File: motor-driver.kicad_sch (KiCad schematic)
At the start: 5 parts, among them J2 Conn_01x02, J3 Conn_01x02, U4 DRV8835

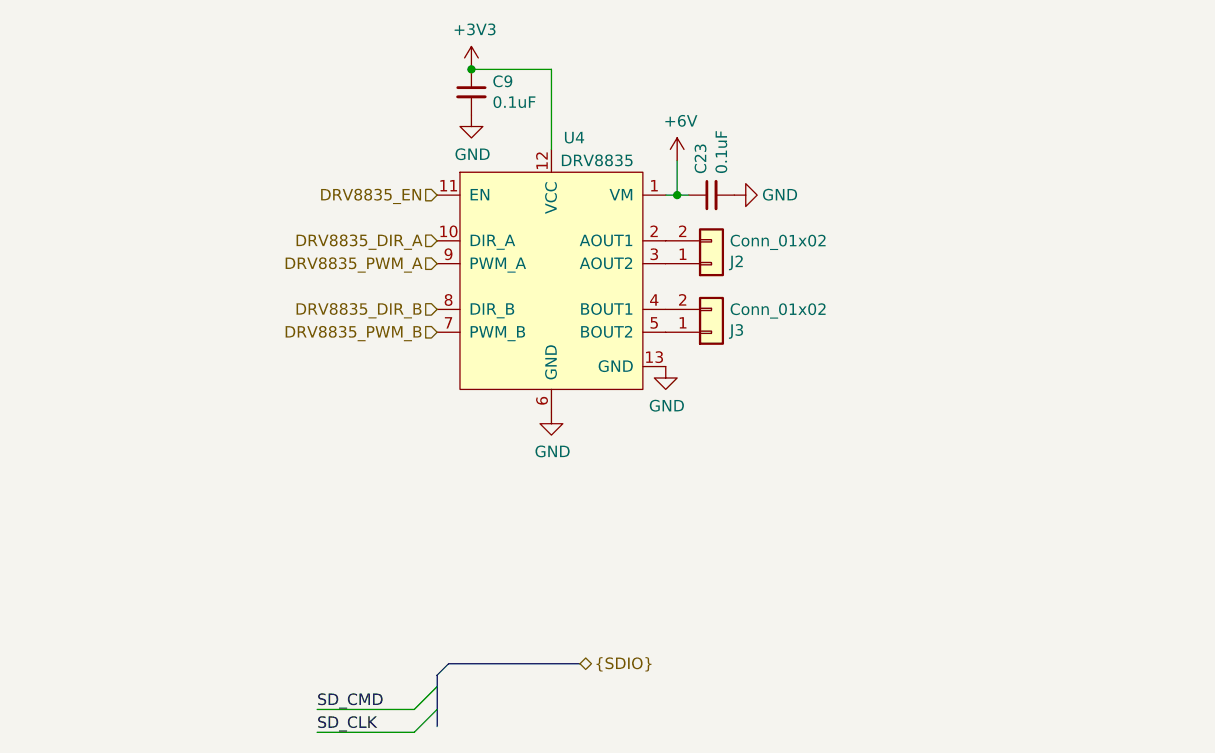
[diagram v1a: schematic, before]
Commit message: Add bus to the motor controller
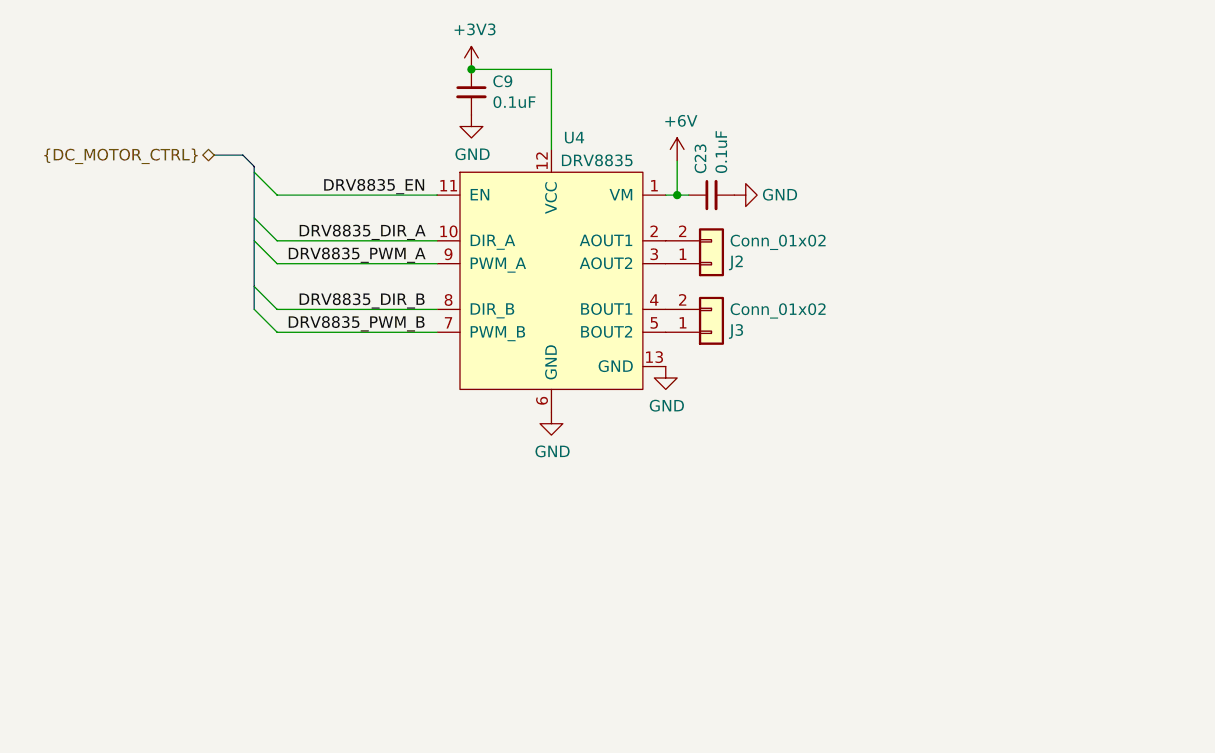
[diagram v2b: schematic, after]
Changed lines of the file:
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@@
   (junction (at 158.75 73.66) (diameter 0) (color 0 0 0 0)
   )
-  (bus_entry (at 132.08 128.27) (size -2.54 2.54)
+  (bus_entry (at 114.3 86.36) (size -2.54 -2.54)
     (stroke (width 0) (type default) (color 0 0 0 0))
   )
-  (bus_entry (at 132.08 130.81) (size -2.54 2.54)
+  (bus_entry (at 114.3 81.28) (size -2.54 -2.54)
+    (stroke (width 0) (type default) (color 0 0 0 0))
+  )
+  (bus_entry (at 114.3 78.74) (size -2.54 -2.54)
+    (stroke (width 0) (type default) (color 0 0 0 0))
+  )
+  (bus_entry (at 114.3 88.9) (size -2.54 -2.54)
+    (stroke (width 0) (type default) (color 0 0 0 0))
+  )
+  (bus_entry (at 114.3 73.66) (size -2.54 -2.54)
     (stroke (width 0) (type default) (color 0 0 0 0))
   )
@@
     (stroke (width 0) (type default) (color 0 0 0 0))
   )
-  (bus (pts (xy 132.08 130.81) (xy 132.08 132.715))
-    (stroke (width 0) (type default) (color 0 0 0 0))
-  )
   (wire (pts (xy 158.75 69.85) (xy 158.75 73.66))
     (stroke (width 0) (type default) (color 0 0 0 0))
   )
-  (bus (pts (xy 133.35 125.73) (xy 132.08 127))
+  (wire (pts (xy 132.08 81.28) (xy 114.3 81.28))
+    (stroke (width 0) (type default) (color 0 0 0 0))
+  )
+  (bus (pts (xy 111.76 70.485) (xy 111.76 71.12))
     (stroke (width 0) (type default) (color 0 0 0 0))
   )
@@
     (stroke (width 0) (type default) (color 0 0 0 0))
   )
-  (bus (pts (xy 132.08 127) (xy 132.08 128.27))
+  (bus (pts (xy 111.76 83.82) (xy 111.76 86.36))
+    (stroke (width 0) (type default) (color 0 0 0 0))
+  )
+  (bus (pts (xy 111.76 71.12) (xy 111.76 76.2))
+    (stroke (width 0) (type default) (color 0 0 0 0))
+  )
+  (wire (pts (xy 132.08 88.9) (xy 114.3 88.9))
+    (stroke (width 0) (type default) (color 0 0 0 0))
+  )
+  (wire (pts (xy 132.08 73.66) (xy 114.3 73.66))
+    (stroke (width 0) (type default) (color 0 0 0 0))
+  )
+  (bus (pts (xy 111.76 76.2) (xy 111.76 78.74))
+    (stroke (width 0) (type default) (color 0 0 0 0))
+  )
+  (bus (pts (xy 111.76 70.485) (xy 110.49 69.215))
+    (stroke (width 0) (type default) (color 0 0 0 0))
+  )
+  (bus (pts (xy 110.49 69.215) (xy 107.315 69.215))
     (stroke (width 0) (type default) (color 0 0 0 0))
   )
@@
     (stroke (width 0) (type default) (color 0 0 0 0))
   )
-  (bus (pts (xy 132.08 128.27) (xy 132.08 130.81))
+  (wire (pts (xy 132.08 86.36) (xy 114.3 86.36))
+    (stroke (width 0) (type default) (color 0 0 0 0))
+  )
+  (bus (pts (xy 111.76 78.74) (xy 111.76 83.82))
     (stroke (width 0) (type default) (color 0 0 0 0))
   )
@@
     (stroke (width 0) (type default) (color 0 0 0 0))
   )
-  (bus (pts (xy 133.35 125.73) (xy 147.955 125.73))
+  (wire (pts (xy 132.08 78.74) (xy 114.3 78.74))
     (stroke (width 0) (type default) (color 0 0 0 0))
   )
-  (wire (pts (xy 129.54 133.35) (xy 118.745 133.35))
-    (stroke (width 0) (type default) (color 0 0 0 0))
+  (label "DRV8835_PWM_B" (at 130.81 88.9 180)
+    (effects (font (size 1.27 1.27)) (justify right bottom))
   )
-  (wire (pts (xy 129.54 130.81) (xy 118.745 130.81))
-    (stroke (width 0) (type default) (color 0 0 0 0))
+  (label "DRV8835_EN" (at 130.81 73.66 180)
+    (effects (font (size 1.27 1.27)) (justify right bottom))
   )
-  (label "SD_CLK" (at 118.745 133.35 0)
-    (effects (font (size 1.27 1.27)) (justify left bottom))
+  (label "DRV8835_DIR_B" (at 130.81 86.36 180)
+    (effects (font (size 1.27 1.27)) (justify right bottom))
   )
-  (label "SD_CMD" (at 118.745 130.81 0)
-    (effects (font (size 1.27 1.27)) (justify left bottom))
+  (label "DRV8835_DIR_A" (at 130.81 78.74 180)
+    (effects (font (size 1.27 1.27)) (justify right bottom))
   )
-  (hierarchical_label "DRV8835_DIR_A" (shape input) (at 132.08 78.74 180)
+  (label "DRV8835_PWM_A" (at 130.81 81.28 180)
+    (effects (font (size 1.27 1.27)) (justify right bottom))
+  )
+  (hierarchical_label "{DC_MOTOR_CTRL}" (shape bidirectional) (at 107.315 69.215 180)
     (effects (font (size 1.27 1.27)) (justify right))
   )
-  (hierarchical_label "DRV8835_EN" (shape input) (at 132.08 73.66 180)
-    (effects (font (size 1.27 1.27)) (justify right))
-  )
-  (hierarchical_label "{SDIO}" (shape bidirectional) (at 147.955 125.73 0)
-    (effects (font (size 1.27 1.27)) (justify left))
-  )
-  (hierarchical_label "DRV8835_DIR_B" (shape input) (at 132.08 86.36 180)
-    (effects (font (size 1.27 1.27)) (justify right))
-  )
-  (hierarchical_label "DRV8835_PWM_B" (shape input) (at 132.08 88.9 180)
-    (effects (font (size 1.27 1.27)) (justify right))
-  )
-  (hierarchical_label "DRV8835_PWM_A" (shape input) (at 132.08 81.28 180)
-    (effects (font (size 1.27 1.27)) (justify right))
-  )

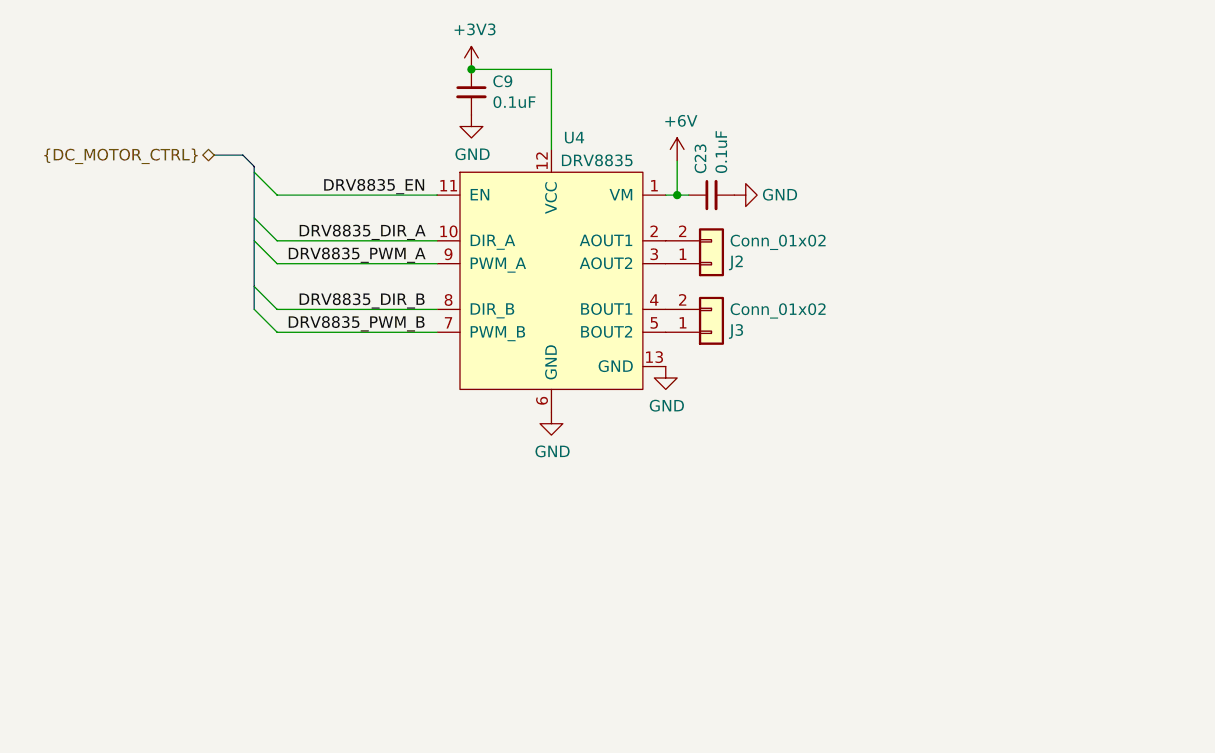
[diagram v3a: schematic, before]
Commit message: Update motor driver symbol, cleanup
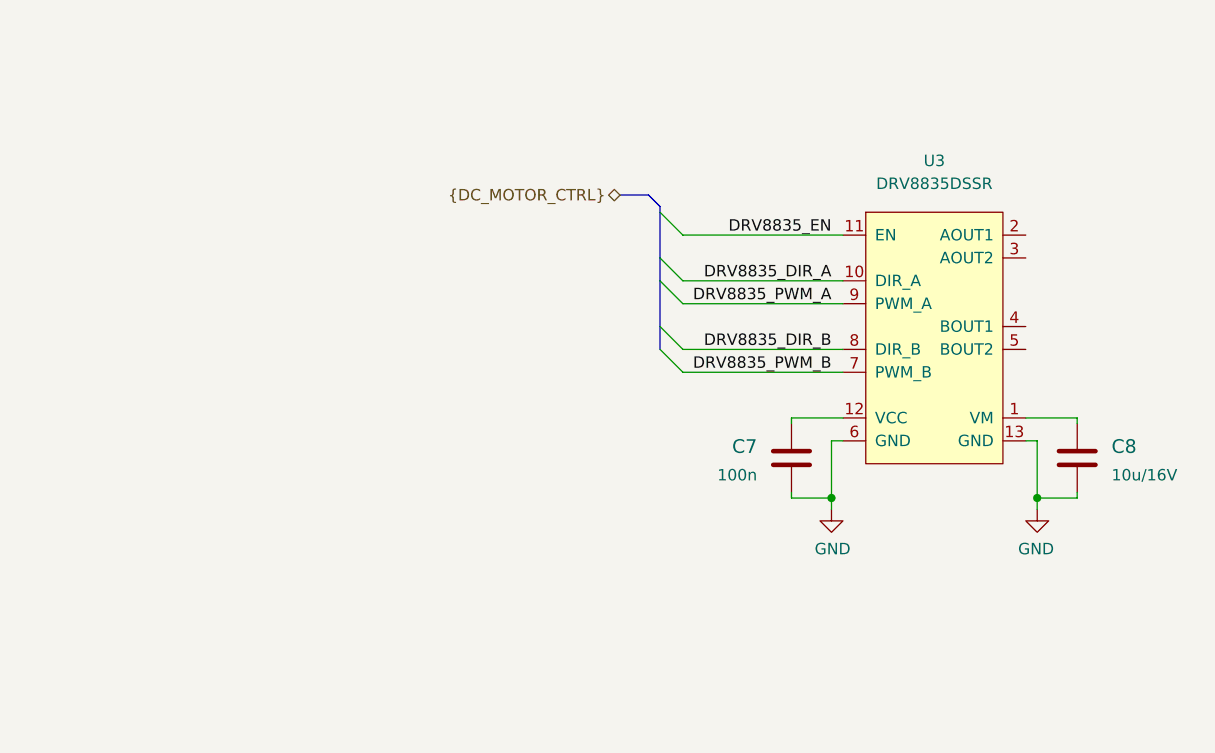
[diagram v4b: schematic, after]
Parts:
- removed C23, C9: 0.1uF, Capacitor_SMD:C_0402_1005Metric, symbol Device:C_Small
- removed J2, J3: Conn_01x02, Connector_PinHeader_1.00mm:PinHeader_1x02_P1.00mm_Vertical, symbol Connector_Generic:Conn_01x02
- removed U4: DRV8835, Package_SON:WSON-12-1EP_3x2mm_P0.5mm_EP1x2.65, symbol drv8835:DRV8835
- added C7: C_100n_0402, antmicro-footprints:0402-cap, symbol antmicroCapacitors0402:C_100n_0402
- added C8: C_10u_16V_0603, antmicro-footprints:0603-cap, symbol antmicroCapacitors0603:C_10u_16V_0603
- added U3: DRV8835DSSR, antmicro-footprints:WSON-12_2x3mm, symbol antmicroPMICMotorDriversControllers:DRV8835DSSR
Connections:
- net DRV8835_DIR_A: now also U3.10 (DIR_A)
- net DRV8835_DIR_B: now also U3.8 (DIR_B)
- net DRV8835_EN: now also U3.11 (EN)
- net DRV8835_PWM_A: now also U3.9 (PWM_A)
- net DRV8835_PWM_B: now also U3.7 (PWM_B)
- net GND: now also C7.2, C8.2, U3.13 (GND), U3.6 (GND)
- new net: C7.1, U3.12 (VCC)
- new net: C8.1, U3.1 (VM)

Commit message: Loclib, cleanup
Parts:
- C7: footprint antmicro-footprints:0402-cap -> synermycha-electronics-footprints:0402-cap; symbol antmicroCapacitors0402:C_100n_0402 -> synermycha-electronics:C_100n_0402
- C8: footprint antmicro-footprints:0603-cap -> synermycha-electronics-footprints:0603-cap; symbol antmicroCapacitors0603:C_10u_16V_0603 -> synermycha-electronics:C_10u_16V_0603
- U3: footprint antmicro-footprints:WSON-12_2x3mm -> synermycha-electronics-footprints:WSON-12_2x3mm; symbol antmicroPMICMotorDriversControllers:DRV8835DSSR -> synermycha-electronics:DRV8835DSSR
